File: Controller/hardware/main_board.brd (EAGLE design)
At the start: 75 x 59 mm, 47 parts, among them IC1 LINEAR_78DT, IC2 40XX_4050D, IC3 LP298XS, IC5 ATMEGA328, U1 CSTNE16M0VH3L000R0, X1 MICROSD_SMD, X4 CON-PHOENIX-508_MST2V

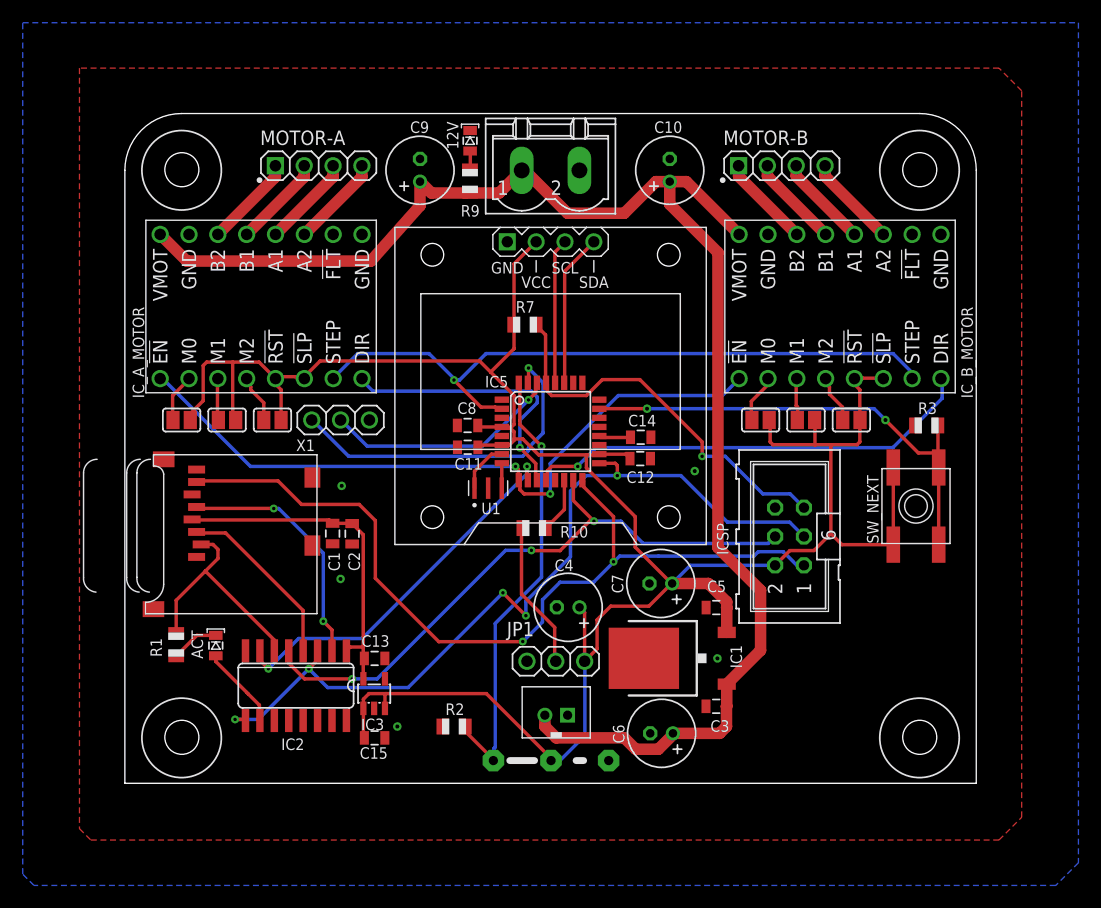
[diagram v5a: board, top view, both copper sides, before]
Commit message: updated board name
updated board name while retaining the original board design files
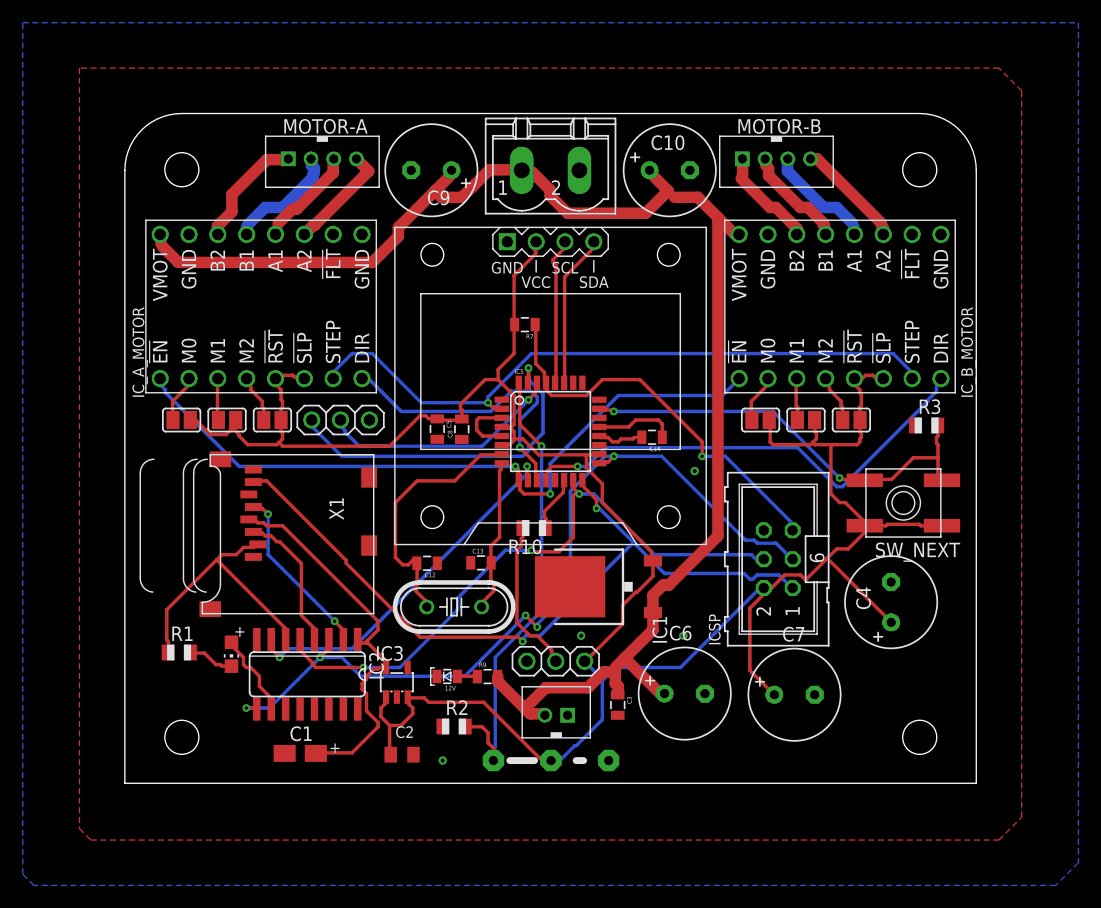
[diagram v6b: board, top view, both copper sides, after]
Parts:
- removed C11: 0.1uF, main_board:SPARKFUN_0805
- removed C15: 1.0uF, main_board:SPARKFUN_0805
- removed U1: CSTNE16M0VH3L000R0, main_board:XTAL_CSTNE16M0VH3L000R0
- added Q4: 16MHZ, crystal:HC49/S
- 12V: value 12v -> (none); device main_board:SPARKFUN_LED-0805 -> SparkFun:LED-0805
- ACT: value ACT -> RED; device main_board:SPARKFUN_LED-0805 -> adafruit:CHIP-LED0805
- C1: value 10uF -> 10uF/10V; device main_board:SPARKFUN_0805 -> adafruit:A/3216-18R
- C10, C4, C6, C7, C9: device main_board:RCL_E3,5-8 -> rcl:E3,5-8
- C12: value 0.1uF -> 16pf; device main_board:SPARKFUN_0805 -> SparkFun:0805
- C13: value 2.2uF -> 16pf; device main_board:SPARKFUN_0805 -> SparkFun:0805
- C14, C3, C5, C8: value 0.1uF -> 100nF; device main_board:SPARKFUN_0805 -> SparkFun:0805
- C2: device main_board:SPARKFUN_0805 -> adafruit:C0805K
- IC1: value LINEAR_78DT -> 7805DT; device main_board:LINEAR_TO252 -> linear:TO252
- IC2: value 40XX_4050D -> 4050D; device main_board:40XX_SO16 -> 40xx:SO16
- IC3: device main_board:ADAFRUIT_SOT23-5L -> adafruit:SOT23-5L
- IC5: device main_board:SPARKFUN_TQFP32-08 -> SparkFun:TQFP32-08
- ICSP: device main_board:CON-HARTING-ML_ML6 -> con-harting-ml:ML6
- IC_A_MOTOR, IC_B_MOTOR: value POLOLU-STEPPER-DRIVER_2133-DRV8825 -> 2133-DRV8825; device main_board:POLOLU-STEPPER-DRIVER_DRV8825 -> pololu-stepper-driver:DRV8825
- J1: device main_board:JUMPER_05C -> jumper:05C
- JP1, JP5: device main_board:ADAFRUIT_1X03 -> adafruit:1X03
- JP4: value JST_EPH_2PIN -> 2PIN; device main_board:JST_EPH_B2B-PH-K-S -> jst_eph:B2B-PH-K-S
- MOTOR-A, MOTOR-B: value (none) -> 4PIN; device main_board:1X04 -> jst_eph:B4B-PH-K-S
- R1: value 1.0k -> 1K; device main_board:ADAFRUIT_R0805 -> adafruit:R0805
- R10: value 330 -> 330r; device main_board:ADAFRUIT_R0805 -> adafruit:R0805
- R2, R3: value 10k -> 10K; device main_board:ADAFRUIT_R0805 -> adafruit:R0805
- R7: value 10k -> 10K; device main_board:ADAFRUIT_R0805 -> SparkFun:0805
- R9: value 2.2k -> 2.2K; device main_board:ADAFRUIT_R0805 -> SparkFun:0805
- SJ1, SJ2, SJ3, SJ4, SJ5, SJ6: device main_board:JUMPER_SJ -> jumper:SJ
- SW_NEXT: device main_board:ADAFRUIT_EVQ-Q2 -> adafruit:EVQ-Q2
- U$1: value DIY-MODULES_DISPLAY-OLED-128X64-I2C -> DISPLAY-OLED-128X64-I2C; device main_board:DIY-MODULES_DISPLAY-OLED-128X64-I2C -> diy-modules:DISPLAY-OLED-128X64-I2C
- X1: value MICROSD_SMD -> MICROSD; device main_board:ADAFRUIT_MICROSD -> adafruit:MICROSD
- X4: value CON-PHOENIX-508_MST2V -> MST2V; device main_board:CON-PHOENIX-508_MSTBV2 -> con-phoenix-508:MSTBV2
- moved 12V 47.2 mm to (28.4, 9.41), turned to 90 degrees
- moved R9 43.7 mm to (31.9, 9.40), turned to 0 degrees
- moved C5 29.2 mm to (27.5, 31.2), turned to 270 degrees
- moved C4 28.5 mm to (67.5, 15.9), turned to 90 degrees
- moved C12 20.9 mm to (26.6, 19.4)
- moved C2 20.0 mm to (24.4, 2.52), turned to 0 degrees
- moved C1 19.6 mm to (15.4, 2.63), turned to 0 degrees
- moved C7 15.3 mm to (59.0, 7.80), turned to 0 degrees
- moved C13 12.6 mm to (31.4, 19.4), turned to 0 degrees
- moved IC1 9.05 mm to (41.7, 17.3)
- moved C3 8.67 mm to (43.4, 6.89), turned to 270 degrees
- moved X1 5.00 mm to (22.0, 28.9)
- moved C6 4.05 mm to (49.3, 7.90), turned to 0 degrees
- moved IC3 2.24 mm to (24.0, 8.90)
- moved ICSP 2.24 mm to (57.5, 19.7)
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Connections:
- removed net N$22: IC5.7, U1.1
- removed net N$23: IC5.8, U1.3
- new net N$31: C12.2, IC5.7, Q4.2
- new net N$32: C13.2, IC5.8, Q4.1
- net +3V3: now also C1.+; no longer C1.1, C13.2, C2.1
- net GND: now also C1.-; no longer C1.2, C11.1, C15.2, U1.2
- net VCC: now also C2.1; no longer C11.2, C12.2, C15.1
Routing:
- net N$31: track 0.00 -> 22.8 mm
- net N$32: track 0.00 -> 13.7 mm
- net GND: track 0.00 -> 12.7 mm, vias 5 -> 4
- net D12: track 75.7 -> 66.8 mm
- net VCC: track 211.7 -> 218.3 mm
- net N$2: track 21.8 -> 15.4 mm
- net A0: track 43.8 -> 38.4 mm
- net +3V3: track 30.1 -> 35.1 mm
- net N$22: track 4.52 -> 0.00 mm
- net N$3: track 20.1 -> 23.8 mm
- net N$5: track 15.8 -> 12.6 mm
- net D8: track 40.1 -> 42.4 mm
- net N$23: track 2.19 -> 0.00 mm
- net N$13: track 8.15 -> 10.3 mm
- net N$14: track 8.15 -> 10.1 mm
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
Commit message: bom and silkscreen updates
bom information added to all the parts and the silkscreen was all normalized to 40mils and placed so there is no more overlapping. a few designators were missing from the board so i brought them back. the only copper change was c1. the old footprint didn't match the part used on the pdf bom.  i modified it to match the designated part.
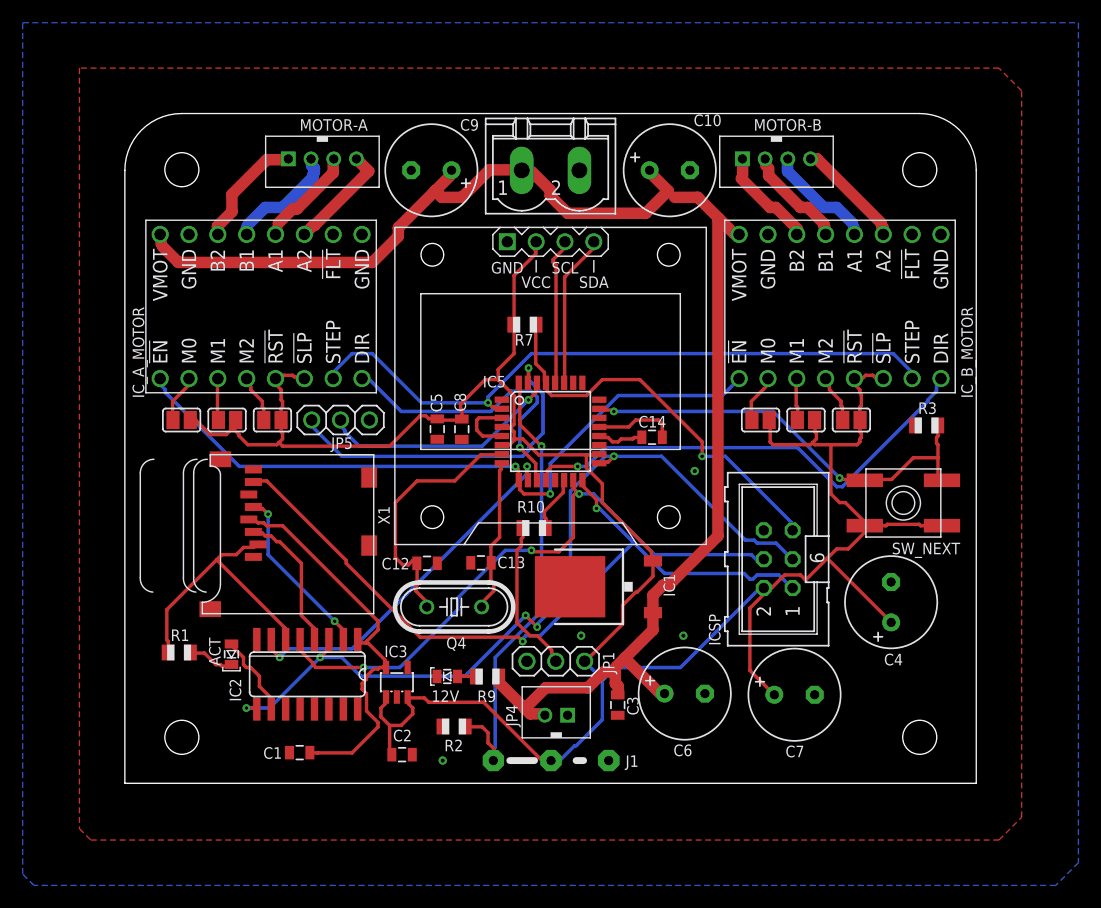
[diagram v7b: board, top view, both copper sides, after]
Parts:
- 12V: device SparkFun:LED-0805 -> main_board:SPARKFUN_LED-0805
- ACT: device adafruit:CHIP-LED0805 -> main_board:SPARKFUN_LED-0805
- C1: value 10uF/10V -> 10uF; device adafruit:A/3216-18R -> main_board:SPARKFUN_0805
- C10, C4, C6, C7, C9: device rcl:E3,5-8 -> main_board:RCL_E3,5-8
- C12, C13: value 16pf -> 16pF; device SparkFun:0805 -> main_board:SPARKFUN_0805
- C14, C3, C5, C8: value 100nF -> 0.1uF; device SparkFun:0805 -> main_board:SPARKFUN_0805
- C2: device adafruit:C0805K -> main_board:SPARKFUN_0805
- IC1: value 7805DT -> LINEAR_78DT; device linear:TO252 -> main_board:LINEAR_TO252
- IC2: value 4050D -> 40XX_4050D; device 40xx:SO16 -> main_board:40XX_SO16
- IC3: device adafruit:SOT23-5L -> main_board:ADAFRUIT_SOT23-5L
- IC5: device SparkFun:TQFP32-08 -> main_board:SPARKFUN_TQFP32-08
- IC_A_MOTOR, IC_B_MOTOR: value 2133-DRV8825 -> POLOLU-STEPPER-DRIVER_2133-DRV8825; device pololu-stepper-driver:DRV8825 -> main_board:POLOLU-STEPPER-DRIVER_DRV8825
- J1: device jumper:05C -> main_board:JUMPER_05C
- Q4: device crystal:HC49/S -> main_board:CRYSTAL_HC49/S
- R1: value 1K -> 1.0k; device adafruit:R0805 -> main_board:ADAFRUIT_R0805
- R10: value 330r -> 330; device adafruit:R0805 -> main_board:ADAFRUIT_R0805
- R2, R3: value 10K -> 10k; device adafruit:R0805 -> main_board:ADAFRUIT_R0805
- R7: value 10K -> 10k; device SparkFun:0805 -> main_board:ADAFRUIT_R0805
- R9: value 2.2K -> 2.2k; device SparkFun:0805 -> main_board:ADAFRUIT_R0805
- SW_NEXT: device adafruit:EVQ-Q2 -> main_board:ADAFRUIT_EVQ-Q2
- U$1: value DISPLAY-OLED-128X64-I2C -> DIY-MODULES_DISPLAY-OLED-128X64-I2C; device diy-modules:DISPLAY-OLED-128X64-I2C -> main_board:DIY-MODULES_DISPLAY-OLED-128X64-I2C
- X1: value MICROSD -> MICROSD_SMD; device adafruit:MICROSD -> main_board:ADAFRUIT_MICROSD
- X4: value MST2V -> CON-PHOENIX-508_MST2V; device con-phoenix-508:MSTBV2 -> main_board:CON-PHOENIX-508_MSTBV2
- moved C1 0.09 mm to (15.4, 2.70), turned to 180 degrees
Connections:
- net +3V3: now also C1.1; no longer C1.+
- net GND: now also C1.2; no longer C1.-
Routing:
- net +3V3: track 35.1 -> 35.6 mm
